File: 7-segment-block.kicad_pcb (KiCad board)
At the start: 2 copper layers, 4 parts, among them J1 DATA_OUT, J2 DATA_IN, U1 TPIC6C596PWR

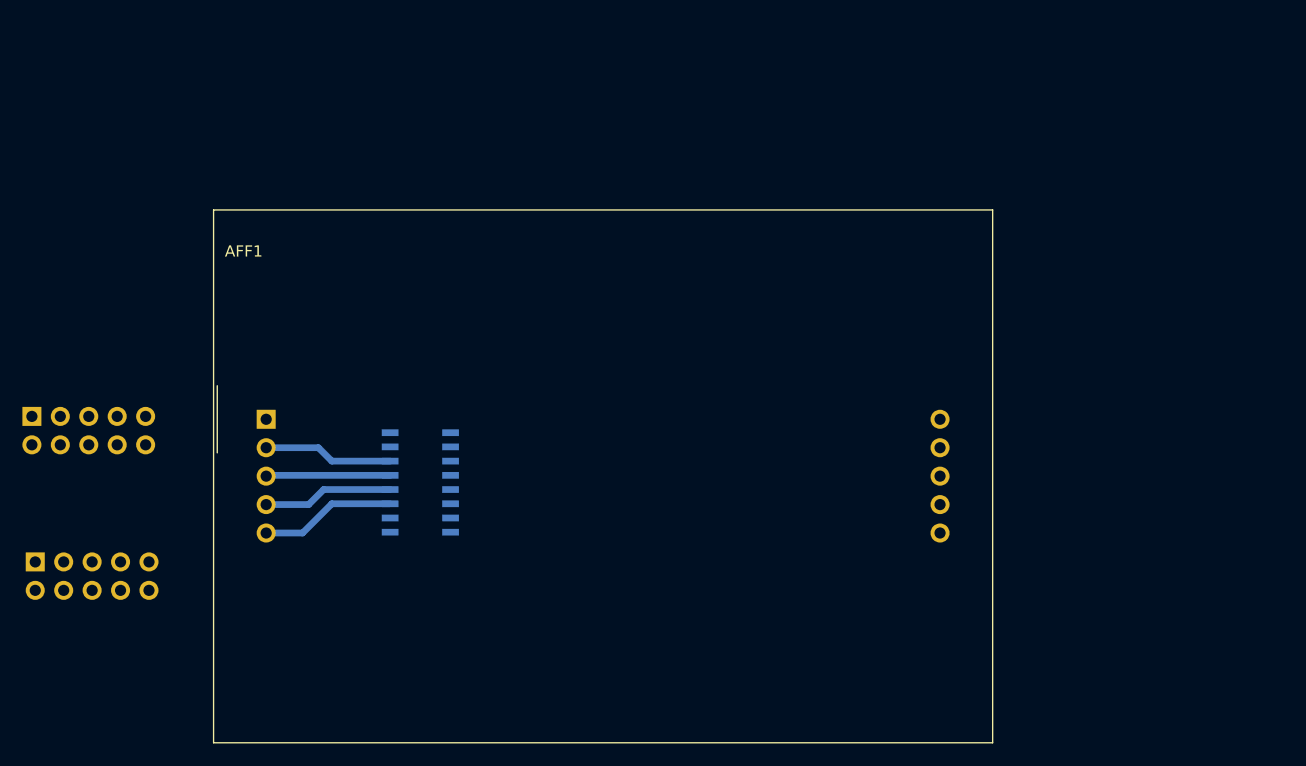
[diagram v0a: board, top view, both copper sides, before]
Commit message: Add mounting holes, dropper resistors and a buffer
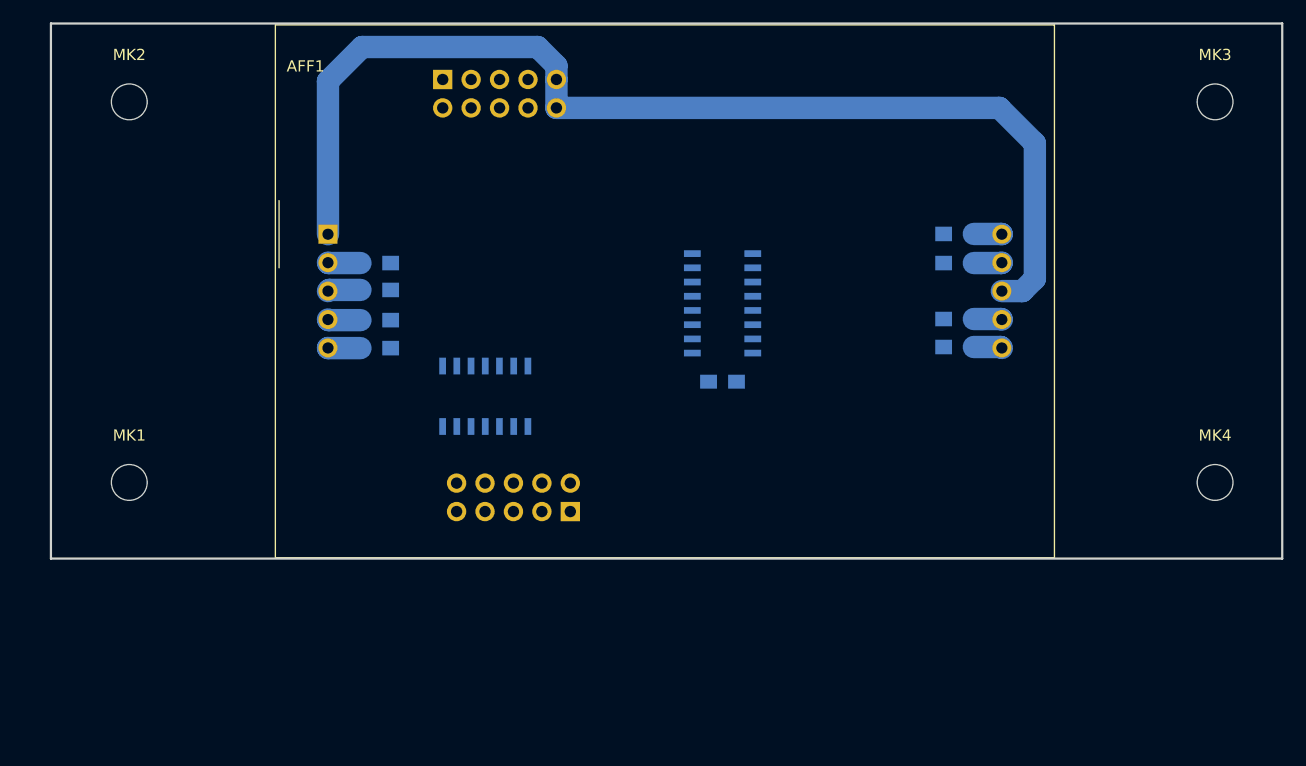
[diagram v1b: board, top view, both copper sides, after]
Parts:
- added C1: C, Capacitors_SMD:C_0805_HandSoldering, B.Cu at (166.0, 76.0)
- added MK1: Mounting_Hole, Mounting_Holes:MountingHole_3.2mm_M3, F.Cu at (113.0, 85.0)
- added MK2: Mounting_Hole, Mounting_Holes:MountingHole_3.2mm_M3, F.Cu at (113.0, 51.0)
- added MK3: Mounting_Hole, Mounting_Holes:MountingHole_3.2mm_M3, F.Cu at (210.0, 51.0)
- added MK4: Mounting_Hole, Mounting_Holes:MountingHole_3.2mm_M3, F.Cu at (210.0, 85.0)
- added R1: 100, Resistors_SMD:R_0805_HandSoldering, B.Cu at (135.0, 73.0)
- added R2: 100, Resistors_SMD:R_0805_HandSoldering, B.Cu at (135.0, 70.5)
- added R3: 100, Resistors_SMD:R_0805_HandSoldering, B.Cu at (135.0, 67.8)
- added R4: 100, Resistors_SMD:R_0805_HandSoldering, B.Cu at (135.0, 65.4)
- added R5: 100, Resistors_SMD:R_0805_HandSoldering, B.Cu at (187.1, 62.8)
- added R6: 100, Resistors_SMD:R_0805_HandSoldering, B.Cu at (187.1, 65.4)
- added R7: 100, Resistors_SMD:R_0805_HandSoldering, B.Cu at (187.1, 70.4)
- added R8: 100, Resistors_SMD:R_0805_HandSoldering, B.Cu at (187.1, 72.9)
- added U2: 74LS125, Housings_SOIC:SOIC-14_3.9x8.7mm_Pitch1.27mm, B.Cu at (144.8, 77.3)
- J1, J2: footprint Connectors_Multicomp:Multicomp_MC9A12-1034_2x05x2.54mm_Straight -> Connectors_IDC:IDC-Header_2x05_Pitch2.54mm_Straight
- moved J2 56.4 mm to (141.0, 49.0), turned to 270 degrees
- moved J1 48.8 mm to (152.4, 87.6), turned to 90 degrees
- moved U1 31.4 mm to (166.0, 69.0)
- moved AFF1 17.4 mm to (130.8, 62.8)
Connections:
- AFF1 pad 1: Net-(AFF1-Pad1) -> VCC
- AFF1 pad 8: Net-(AFF1-Pad8) -> VCC
- J1 pad 4: /RCK -> Net-(J1-Pad4)
- J1 pad 6: /SRCK -> Net-(J1-Pad6)
- J1 pad 7: /~G -> GND
- J1 pad 8: GND -> Net-(J1-Pad8)
- J2 pad 7: /~G -> GND
- J2 pad 8: GND -> /~G
- U1 pad 11: Net-(AFF1-Pad10) -> Net-(R5-Pad2)
- U1 pad 12: Net-(AFF1-Pad9) -> Net-(R6-Pad2)
- U1 pad 13: Net-(AFF1-Pad7) -> Net-(R7-Pad2)
- U1 pad 14: Net-(AFF1-Pad6) -> Net-(R8-Pad2)
- U1 pad 3: Net-(AFF1-Pad5) -> Net-(R1-Pad2)
- U1 pad 4: Net-(AFF1-Pad4) -> Net-(R2-Pad2)
- U1 pad 5: Net-(AFF1-Pad3) -> Net-(R3-Pad2)
- U1 pad 6: Net-(AFF1-Pad2) -> Net-(R4-Pad2)
- U1 pad 9: Net-(J1-Pad2) -> Net-(U1-Pad9)
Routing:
- net VCC: track 0.00 -> 99.4 mm
- net Net-(AFF1-Pad5): track 12.2 -> 2.91 mm
- net Net-(AFF1-Pad4): track 11.6 -> 2.92 mm
- net Net-(AFF1-Pad2): track 11.6 -> 2.91 mm
- net Net-(AFF1-Pad3): track 11.1 -> 2.94 mm
- net Net-(AFF1-Pad6): track 0.00 -> 2.54 mm
- net Net-(AFF1-Pad7): track 0.00 -> 2.52 mm
- net Net-(AFF1-Pad9): track 0.00 -> 2.51 mm
- net Net-(AFF1-Pad10): track 0.00 -> 2.51 mm
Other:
- board outline added: 110 x 47.8 mm

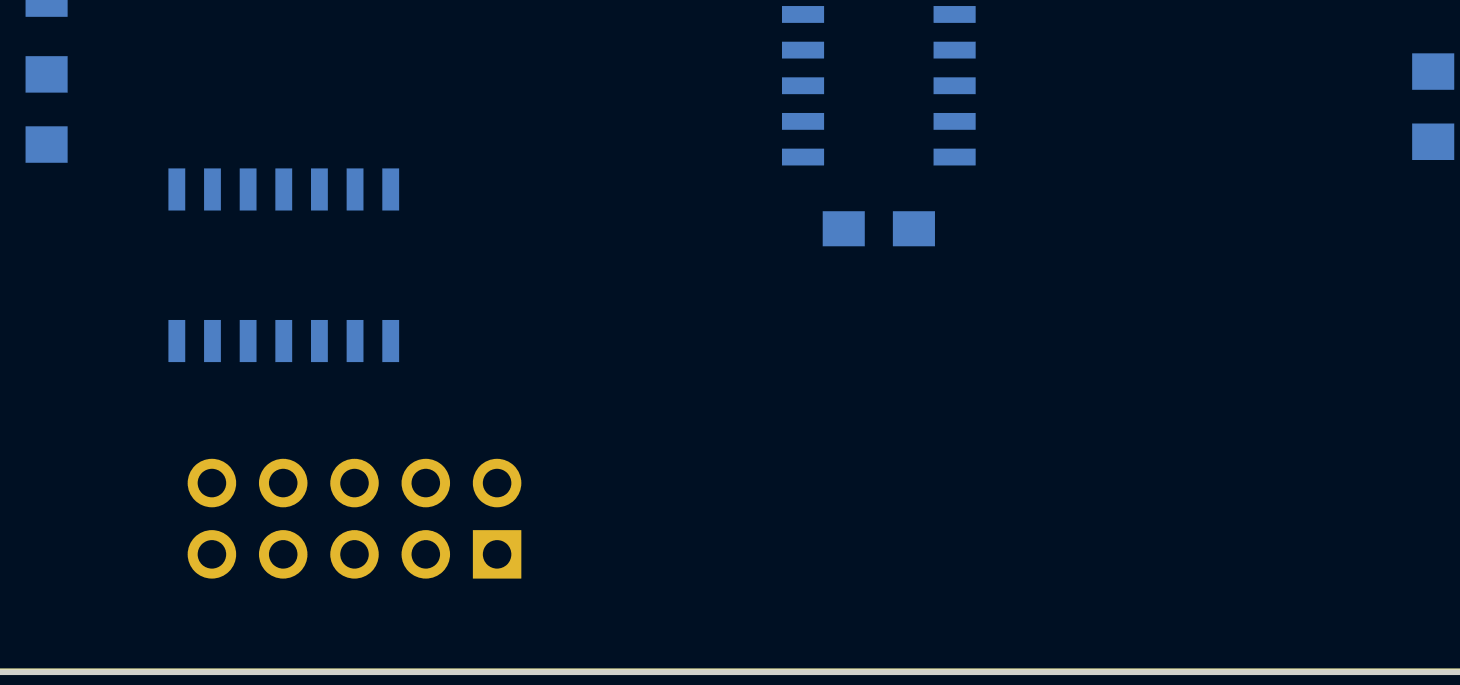
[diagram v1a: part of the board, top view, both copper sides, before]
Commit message: Add terminator resistors
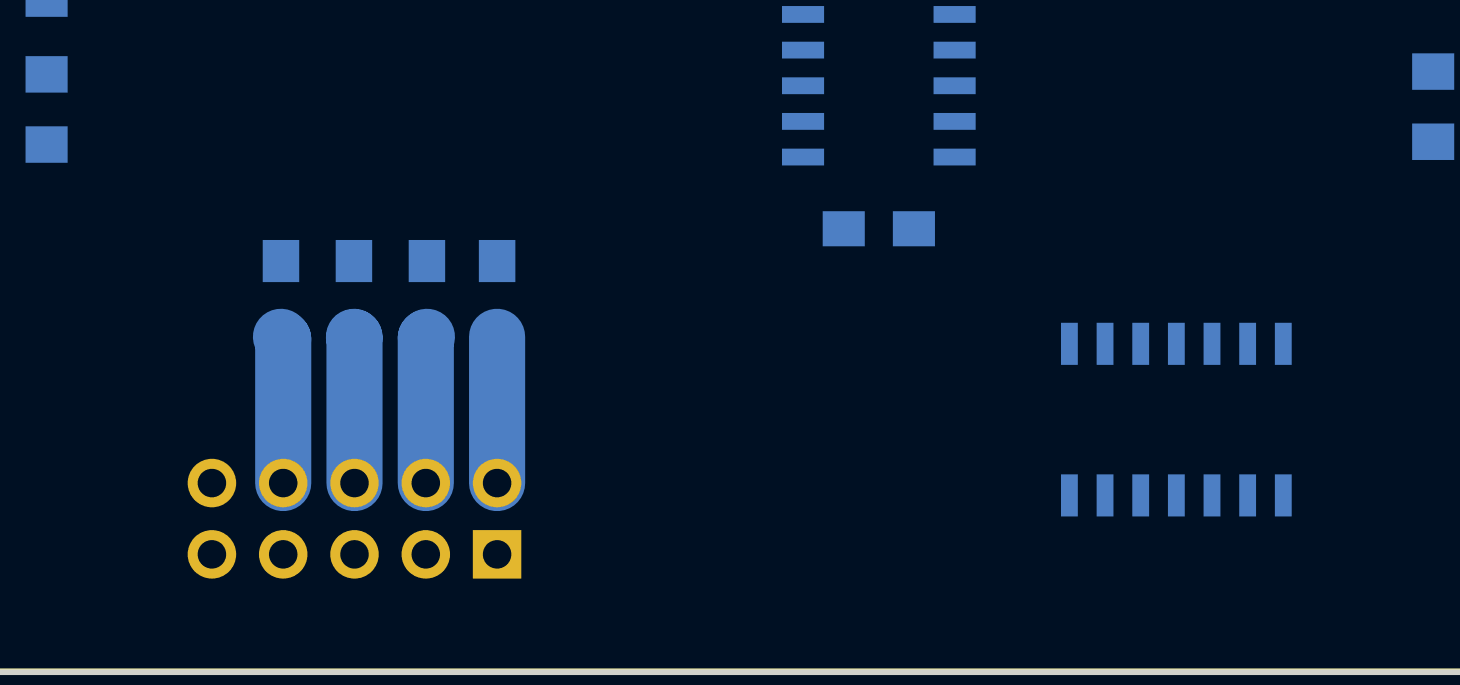
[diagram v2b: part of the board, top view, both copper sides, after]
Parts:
- added R10: 100, Resistors_SMD:R_0805_HandSoldering, B.Cu at (149.9, 78.5)
- added R11: 100, Resistors_SMD:R_0805_HandSoldering, B.Cu at (147.3, 78.5)
- added R12: 100, Resistors_SMD:R_0805_HandSoldering, B.Cu at (144.7, 78.5)
- added R9: 100, Resistors_SMD:R_0805_HandSoldering, B.Cu at (152.4, 78.5)
- moved U2 32.3 mm to (176.6, 82.8)
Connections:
- U2 pad 11: Net-(J1-Pad8) -> Net-(R12-Pad1)
- U2 pad 3: Net-(J1-Pad2) -> Net-(R9-Pad1)
- U2 pad 6: Net-(J1-Pad4) -> Net-(R10-Pad1)
- U2 pad 8: Net-(J1-Pad6) -> Net-(R11-Pad1)
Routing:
- net Net-(J1-Pad8): track 0.00 -> 5.24 mm
- net Net-(J1-Pad4): track 0.00 -> 5.23 mm
- net Net-(J1-Pad6): track 0.00 -> 5.22 mm
- net Net-(J1-Pad2): track 0.00 -> 5.21 mm

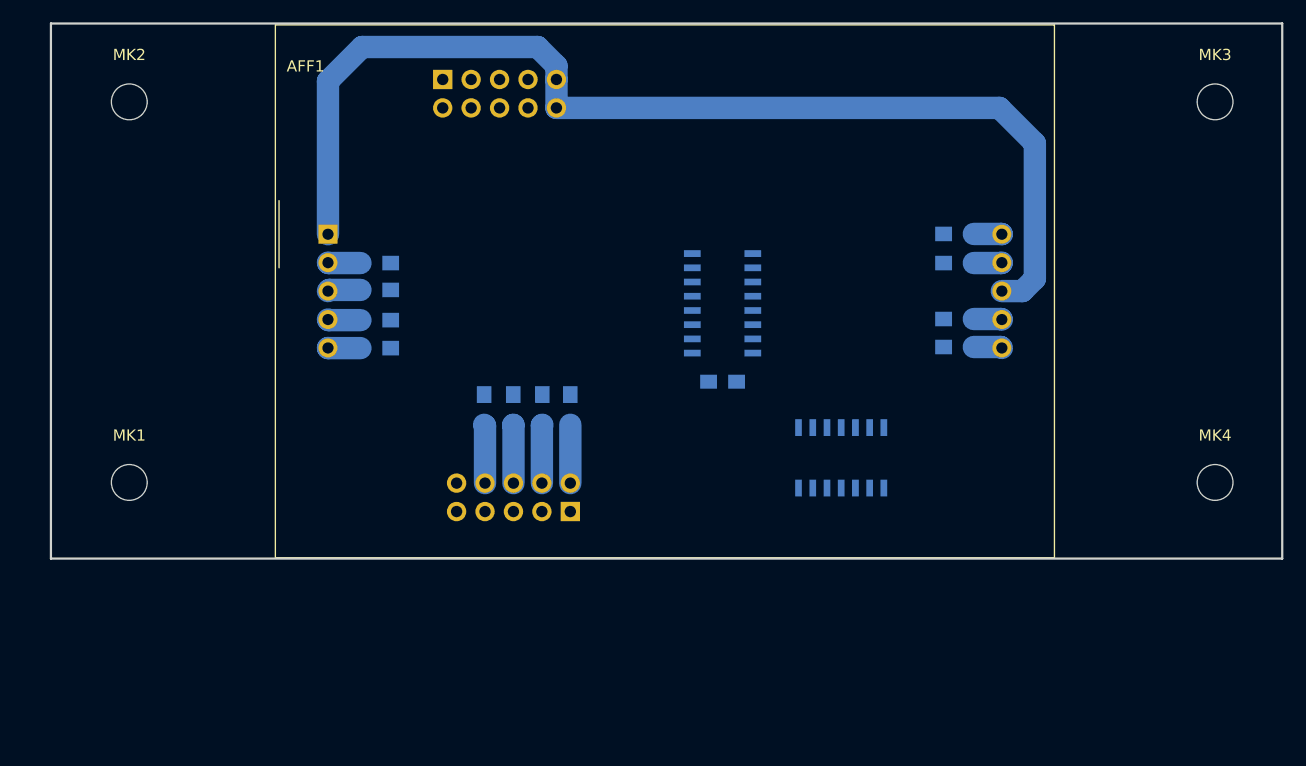
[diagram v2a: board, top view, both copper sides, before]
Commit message: Start routing, maybe change to a different buffer that has a more friendly pin location
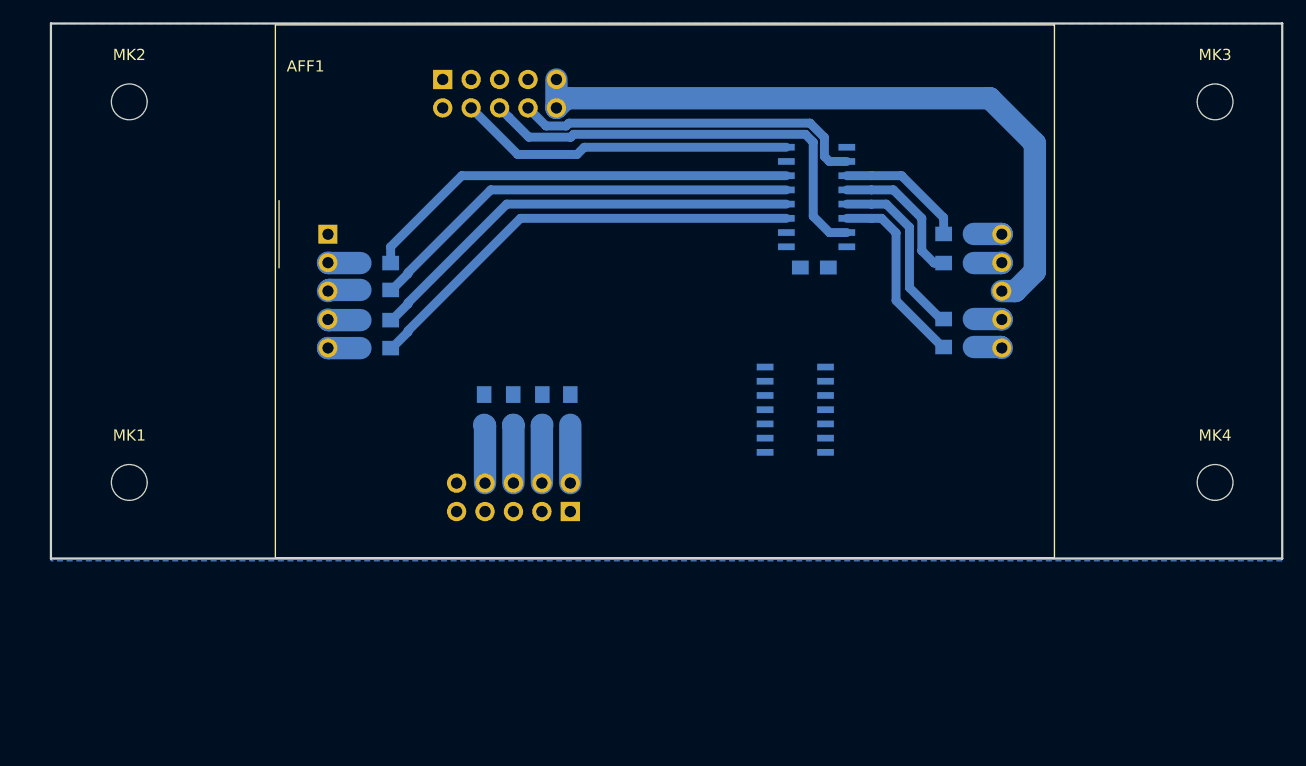
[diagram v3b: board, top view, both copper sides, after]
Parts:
- moved C1 13.1 mm to (174.2, 65.8)
- moved U1 12.7 mm to (174.4, 59.5)
- moved U2 5.94 mm to (172.5, 78.5), turned to 0 degrees
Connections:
- net Net-(U1-Pad9) renamed /SER_OUT
- J2 pad 4: /RCK -> /~G
- J2 pad 8: /~G -> /RCK
- U2 pad 12: /~G -> /RCK
- U2 pad 5: /RCK -> /~G
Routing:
- net Net-(R1-Pad2): track 0.00 -> 40.2 mm
- net /SRCK: track 0.00 -> 39.7 mm
- net Net-(R2-Pad2): track 0.00 -> 39.7 mm
- net Net-(R4-Pad2): track 0.00 -> 39.4 mm
- net Net-(R3-Pad2): track 0.00 -> 39.1 mm
- net VCC: track 99.4 -> 62.4 mm
- net /RCK: track 0.00 -> 31.7 mm
- net /~G: track 0.00 -> 30.2 mm
- net Net-(R8-Pad2): track 0.00 -> 17.0 mm
- net Net-(R7-Pad2): track 0.00 -> 16.1 mm
- net Net-(R6-Pad2): track 0.00 -> 13.1 mm
- net Net-(R5-Pad2): track 0.00 -> 11.7 mm
- added copper zone on B.Cu, net GND

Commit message: Finish routing, change buffer IC, add some decoupling caps
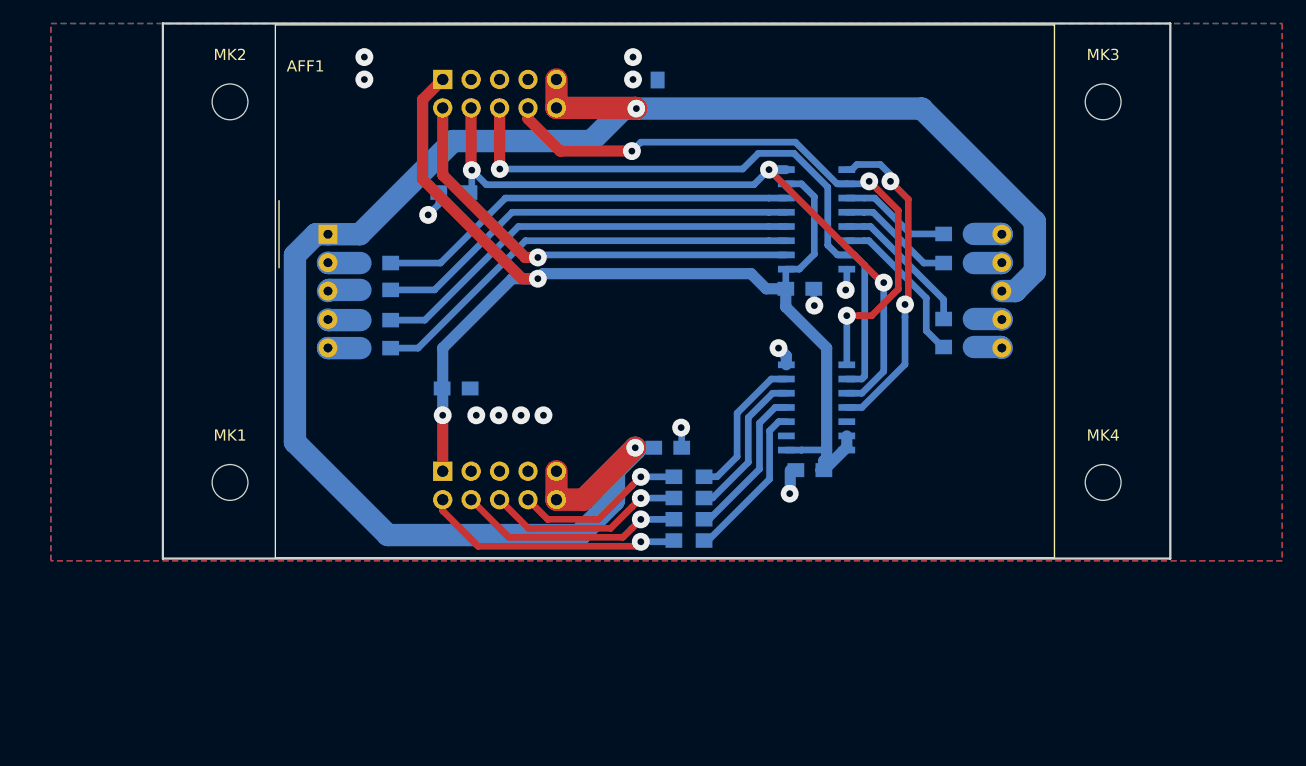
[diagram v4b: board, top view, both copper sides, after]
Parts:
- added C2: C, Capacitors_SMD:C_0805_HandSoldering, B.Cu at (173.8, 83.9)
- added C4: C, Capacitors_SMD:C_0805_HandSoldering, B.Cu at (160.2, 50.3)
- added C5: C, Capacitors_SMD:C_0805_HandSoldering, B.Cu at (142.2, 76.6)
- added C6: C, Capacitors_SMD:C_0805_HandSoldering, B.Cu at (161.1, 81.9)
- added R13: 10k, Resistors_SMD:R_0805_HandSoldering, B.Cu at (142.0, 59.1)
- R1: value 100 -> 90
- R2, R3, R4, R5, R6, R7, R8: value 100 -> 180
- U2: value 74LS125 -> 74LS243
- moved R12 19.3 mm to (163.0, 84.5), turned to 180 degrees
- moved R11 17.6 mm to (163.0, 86.4), turned to 180 degrees
- moved R10 16.4 mm to (163.0, 88.3), turned to 180 degrees
- moved R9 15.8 mm to (163.0, 90.2), turned to 180 degrees
- moved J1 12.0 mm to (141.0, 84.0), turned to 270 degrees
- moved MK3 10.0 mm to (200.0, 51.0)
- moved MK4 10.0 mm to (200.0, 85.0)
- moved MK1 9.00 mm to (122.0, 85.0)
- moved MK2 9.00 mm to (122.0, 51.0)
- moved C1 2.30 mm to (172.9, 67.7)
- moved U1 2.00 mm to (174.4, 61.5)
- moved U2 1.91 mm to (174.4, 78.3)
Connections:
- net Net-(AFF1-Pad10) renamed /SEG_G
- net Net-(AFF1-Pad2) renamed /SEG_E
- net Net-(AFF1-Pad3) renamed /SEG_D
- net Net-(AFF1-Pad4) renamed /SEG_C
- net Net-(AFF1-Pad5) renamed /SEG_DP
- net Net-(AFF1-Pad6) renamed /SEG_B
- net Net-(AFF1-Pad7) renamed /SEG_A
- net Net-(AFF1-Pad9) renamed /SEG_F
- U1 pad 7: Net-(U1-Pad7) -> +5V
- U2 pad 1: GND -> +5V
- U2 pad 10: GND -> /~G
- U2 pad 11: Net-(R12-Pad1) -> /SER_OUT
- U2 pad 12: /RCK -> (no net)
- U2 pad 13: GND -> +5V
- U2 pad 14: (no net) -> +5V
- U2 pad 2: /SER_OUT -> (no net)
- U2 pad 4: GND -> Net-(R10-Pad1)
- U2 pad 5: /~G -> Net-(R11-Pad1)
- U2 pad 6: Net-(R10-Pad1) -> Net-(R12-Pad1)
- U2 pad 7: (no net) -> GND
- U2 pad 8: Net-(R11-Pad1) -> /RCK
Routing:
- net +5V: track 0.00 -> 113.8 mm, vias 0 -> 2
- net VCC: track 62.4 -> 164.0 mm, vias 0 -> 2
- net /SER_IN: track 0.00 -> 39.8 mm, vias 0 -> 1
- net /~G: track 30.2 -> 63.4 mm, vias 0 -> 3
- net /SER_OUT: track 0.00 -> 29.0 mm, vias 0 -> 2
- net /RCK: track 31.7 -> 55.3 mm, vias 0 -> 3
- net Net-(J1-Pad2): track 5.21 -> 23.2 mm, vias 0 -> 1
- net /SRCK: track 39.7 -> 57.4 mm, vias 0 -> 1
- net Net-(J1-Pad4): track 5.23 -> 20.2 mm, vias 0 -> 1
- net Net-(R9-Pad1): track 0.00 -> 14.3 mm
- net Net-(R10-Pad1): track 0.00 -> 13.9 mm
- net Net-(R11-Pad1): track 0.00 -> 13.6 mm
- net Net-(R12-Pad1): track 0.00 -> 13.2 mm
- net Net-(J1-Pad6): track 5.22 -> 17.8 mm, vias 0 -> 1
- net GND: track 0.00 -> 11.5 mm, vias 0 -> 14
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- added copper zone on F.Cu, net GND
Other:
- board size 110 x 47.8 mm -> 90 x 47.8 mm
